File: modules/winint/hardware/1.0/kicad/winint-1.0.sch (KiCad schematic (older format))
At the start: 56 parts, among them J1 Screw_Terminal_01x09, J2 Screw_Terminal_01x09, J3 M12-5PIN, J4 RELAYS, K1 SANYOU_SRD_Form_C, K2 SANYOU_SRD_Form_C, Q1 2N2219, Q2 2N2219, SW1 INSTANCE, U1 PC817, U2 PC817, U3 PC817, U4 PC817, U5 PC817, U6 PC817, U7 Teensy_3.2, U8 TEC2-2411WI, U9 MCP2551-I-P

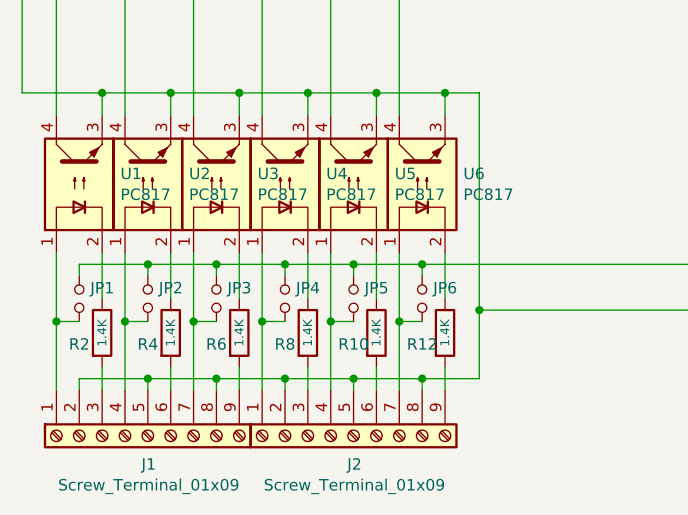
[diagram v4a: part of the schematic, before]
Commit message: Revised PCB layout
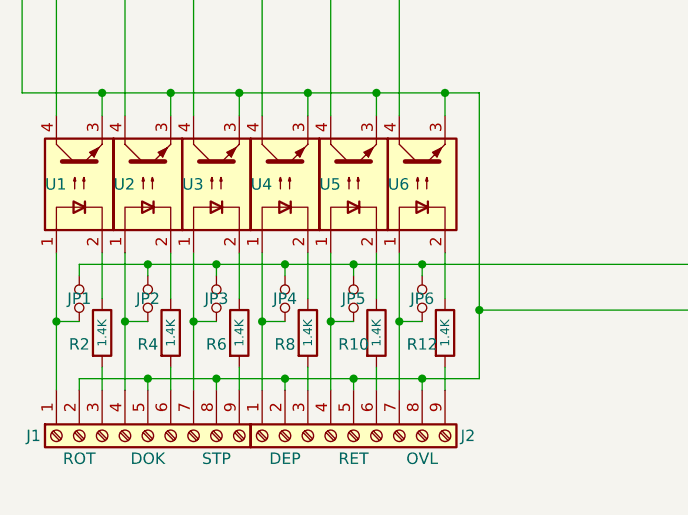
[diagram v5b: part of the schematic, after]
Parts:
- U1: value PC817 -> ROT
- U2: value PC817 -> DOK
- U3: value PC817 -> STP
- U4: value PC817 -> DEP
- U5: value PC817 -> RET
- U6: value PC817 -> OVL
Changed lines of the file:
@@
 U 1 1 60265696
 P 1100 6150
-F 0 "JP1" V 1146 6102 50  0000 R CNN
+F 0 "JP1" V 1100 6150 50  0000 C CNN
 F 1 "SCR" V 1055 6102 50  0001 R CNN
 F 2 "Connector_PinHeader_2.54mm:PinHeader_1x02_P2.54mm_Vertical" H 1100 6150 50  0001 C CNN
@@
 U 1 1 6026A113
 P 1400 6150
-F 0 "JP2" V 1446 6102 50  0000 R CNN
+F 0 "JP2" V 1400 6150 50  0000 C CNN
 F 1 "SCR" V 1355 6102 50  0001 R CNN
 F 2 "Connector_PinHeader_2.54mm:PinHeader_1x02_P2.54mm_Vertical" H 1400 6150 50  0001 C CNN
@@
 U 1 1 6026A739
 P 1700 6150
-F 0 "JP3" V 1746 6102 50  0000 R CNN
+F 0 "JP3" V 1700 6150 50  0000 C CNN
 F 1 "SCR" V 1655 6102 50  0001 R CNN
 F 2 "Connector_PinHeader_2.54mm:PinHeader_1x02_P2.54mm_Vertical" H 1700 6150 50  0001 C CNN
@@
 U 1 1 6026ABE4
 P 2000 6150
-F 0 "JP4" V 2046 6102 50  0000 R CNN
+F 0 "JP4" V 2000 6150 50  0000 C CNN
 F 1 "SCR" V 1955 6102 50  0001 R CNN
 F 2 "Connector_PinHeader_2.54mm:PinHeader_1x02_P2.54mm_Vertical" H 2000 6150 50  0001 C CNN
@@
 U 1 1 6026E0BA
 P 2300 6150
-F 0 "JP5" V 2346 6102 50  0000 R CNN
+F 0 "JP5" V 2300 6150 50  0000 C CNN
 F 1 "SCR" V 2255 6102 50  0001 R CNN
 F 2 "Connector_PinHeader_2.54mm:PinHeader_1x02_P2.54mm_Vertical" H 2300 6150 50  0001 C CNN
@@
 U 1 1 6026E6CF
 P 2600 6150
-F 0 "JP6" V 2646 6102 50  0000 R CNN
+F 0 "JP6" V 2600 6150 50  0000 C CNN
 F 1 "SCR" V 2555 6102 50  0001 R CNN
 F 2 "Connector_PinHeader_2.54mm:PinHeader_1x02_P2.54mm_Vertical" H 2600 6150 50  0001 C CNN
@@
 U 1 1 5FBA893A
 P 1400 6750
-F 0 "J1" V 1525 6746 50  0000 C CNN
-F 1 "Screw_Terminal_01x09" V 1616 6746 50  0000 C CNN
+F 0 "J1" V 1400 7250 50  0000 C CNN
+F 1 "Screw_Terminal_01x09" V 1616 6746 50  0001 C CNN
 F 2 "TerminalBlock_Phoenix:TerminalBlock_Phoenix_MPT-0,5-9-2.54_1x09_P2.54mm_Horizontal" H 1400 6750 50  0001 C CNN
 F 3 "~" H 1400 6750 50  0001 C CNN
@@
 U 1 1 5FBB1A89
 P 2300 6750
-F 0 "J2" V 2425 6746 50  0000 C CNN
-F 1 "Screw_Terminal_01x09" V 2516 6746 50  0000 C CNN
+F 0 "J2" V 2300 6250 50  0000 C CNN
+F 1 "Screw_Terminal_01x09" V 2516 6746 50  0001 C CNN
 F 2 "TerminalBlock_Phoenix:TerminalBlock_Phoenix_MPT-0,5-9-2.54_1x09_P2.54mm_Horizontal" H 2300 6750 50  0001 C CNN
 F 3 "~" H 2300 6750 50  0001 C CNN
@@
 U 1 1 5FBBA210
 P 1100 5650
-F 0 "U1" V 1146 5470 50  0000 R CNN
-F 1 "PC817" V 1055 5470 50  0000 R CNN
+F 0 "U1" V 1100 5800 50  0000 R CNN
+F 1 "ROT" V -100 5650 50  0000 C CNN
 F 2 "Package_DIP:DIP-4_W7.62mm" H 900 5450 50  0001 L CIN
 F 3 "http://www.soselectronic.cz/a_info/resource/d/pc817.pdf" H 1100 5650 50  0001 L CNN
@@
 U 1 1 5FBBFA82
 P 1400 5650
-F 0 "U2" V 1446 5470 50  0000 R CNN
-F 1 "PC817" V 1355 5470 50  0000 R CNN
+F 0 "U2" V 1400 5800 50  0000 R CNN
+F 1 "DOK" V 200 5650 50  0000 C CNN
 F 2 "Package_DIP:DIP-4_W7.62mm" H 1200 5450 50  0001 L CIN
 F 3 "http://www.soselectronic.cz/a_info/resource/d/pc817.pdf" H 1400 5650 50  0001 L CNN
@@
 U 1 1 5FBC043C
 P 1700 5650
-F 0 "U3" V 1746 5470 50  0000 R CNN
-F 1 "PC817" V 1655 5470 50  0000 R CNN
+F 0 "U3" V 1700 5800 50  0000 R CNN
+F 1 "STP" V 500 5650 50  0000 C CNN
 F 2 "Package_DIP:DIP-4_W7.62mm" H 1500 5450 50  0001 L CIN
 F 3 "http://www.soselectronic.cz/a_info/resource/d/pc817.pdf" H 1700 5650 50  0001 L CNN
@@
 U 1 1 5FBC0B0F
 P 2000 5650
-F 0 "U4" V 2046 5470 50  0000 R CNN
-F 1 "PC817" V 1955 5470 50  0000 R CNN
+F 0 "U4" V 2000 5800 50  0000 R CNN
+F 1 "DEP" V 800 5650 50  0000 C CNN
 F 2 "Package_DIP:DIP-4_W7.62mm" H 1800 5450 50  0001 L CIN
 F 3 "http://www.soselectronic.cz/a_info/resource/d/pc817.pdf" H 2000 5650 50  0001 L CNN
@@
 U 1 1 5FBC14DB
 P 2300 5650
-F 0 "U5" V 2346 5470 50  0000 R CNN
-F 1 "PC817" V 2255 5470 50  0000 R CNN
+F 0 "U5" V 2300 5800 50  0000 R CNN
+F 1 "RET" V 1100 5650 50  0000 C CNN
 F 2 "Package_DIP:DIP-4_W7.62mm" H 2100 5450 50  0001 L CIN
 F 3 "http://www.soselectronic.cz/a_info/resource/d/pc817.pdf" H 2300 5650 50  0001 L CNN
@@
 U 1 1 5FBC1BCF
 P 2600 5650
-F 0 "U6" V 2646 5470 50  0000 R CNN
-F 1 "PC817" V 2555 5470 50  0000 R CNN
+F 0 "U6" V 2600 5800 50  0000 R CNN
+F 1 "OVL" V 1400 5650 50  0000 C CNN
 F 2 "Package_DIP:DIP-4_W7.62mm" H 2400 5450 50  0001 L CIN
 F 3 "http://www.soselectronic.cz/a_info/resource/d/pc817.pdf" H 2600 5650 50  0001 L CNN
@@
 	4900 3300 5100 3300
 $Comp
-L power:GND #PWR?
+L power:GND #PWR0101
 U 1 1 5FD8D24E
 P 5000 6200
-F 0 "#PWR?" H 5000 5950 50  0001 C CNN
+F 0 "#PWR0101" H 5000 5950 50  0001 C CNN
 F 1 "GND" H 5005 6027 50  0000 C CNN
 F 2 "" H 5000 6200 50  0001 C CNN

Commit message: Tidy up
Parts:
- R15: value 200R, 125mW -> 200R
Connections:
- no-connect marks 2 -> 9
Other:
- moved on the sheet: SW1
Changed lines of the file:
@@
 U 1 1 5F1E6C5E
 P 7300 5600
-F 0 "R16" H 7400 5550 50  0000 C CNN
-F 1 "4K7" H 7450 5650 50  0000 C CNN
+F 0 "R16" H 7200 5450 50  0000 C CNN
+F 1 "4K7" V 7300 5600 39  0000 C CNN
 F 2 "Resistor_THT:R_Axial_DIN0204_L3.6mm_D1.6mm_P2.54mm_Vertical" V 7230 5600 50  0001 C CNN
 F 3 "~" H 7300 5600 50  0001 C CNN
@@
 U 1 1 5F21EFF3
 P 9100 5600
-F 0 "R20" H 9000 5550 50  0000 C CNN
-F 1 "100R" H 8950 5650 50  0000 C CNN
+F 0 "R20" H 9000 5450 50  0000 C CNN
+F 1 "100R" V 9100 5600 39  0000 C CNN
 F 2 "Resistor_THT:R_Axial_DIN0204_L3.6mm_D1.6mm_P5.08mm_Horizontal" V 9030 5600 50  0001 C CNN
 F 3 "~" H 9100 5600 50  0001 C CNN
@@
 U 1 1 5F21F397
 P 8700 5600
-F 0 "R19" H 8800 5650 50  0000 C CNN
-F 1 "100R" H 8850 5550 50  0000 C CNN
+F 0 "R19" H 8800 5750 50  0000 C CNN
+F 1 "100R" V 8700 5600 39  0000 C CNN
 F 2 "Resistor_THT:R_Axial_DIN0204_L3.6mm_D1.6mm_P5.08mm_Horizontal" V 8630 5600 50  0001 C CNN
 F 3 "~" H 8700 5600 50  0001 C CNN
@@
 	9100 4950 9100 5450
 Wire Wire Line
-	7300 6200 7400 6200
+	7300 6200 7100 6200
 Wire Wire Line
 	9100 6200 9100 6050
@@
 Connection ~ 7300 6200
 Wire Wire Line
-	950  1450 850  1450
-Wire Wire Line
-	850  1450 850  1550
-Wire Wire Line
-	950  1550 850  1550
-Connection ~ 850  1550
-Wire Wire Line
-	850  1550 850  1650
-Wire Wire Line
-	950  1650 850  1650
-Connection ~ 850  1650
-Wire Wire Line
-	850  1650 850  1750
-Wire Wire Line
-	950  1750 850  1750
-Connection ~ 850  1750
-Wire Wire Line
-	850  1750 850  1850
-Wire Wire Line
-	950  1850 850  1850
-Connection ~ 850  1850
-Wire Wire Line
-	850  1850 850  1950
-Wire Wire Line
-	950  1950 850  1950
-Connection ~ 850  1950
-Wire Wire Line
-	850  1950 850  2050
-Wire Wire Line
-	950  2050 850  2050
-Connection ~ 850  2050
-Wire Wire Line
 	9100 4350 9100 3650
 Wire Wire Line
 	9100 3650 8500 3650
 Wire Wire Line
-	7500 4050 7400 4050
+	7500 4050 7100 4050
 Connection ~ 8700 4750
 Connection ~ 9100 4950
@@
 Wire Wire Line
 	8500 4950 9100 4950
-Connection ~ 7400 6200
+Connection ~ 7100 6200
 Wire Wire Line
 	7500 3650 7200 3650
@@
 	7200 3650 7200 2900
 Connection ~ 7200 3650
-Wire Wire Line
-	7400 6200 8550 6200
 $Comp
 L Device:Polyfuse_Small F1
@@
 Connection ~ 6850 6200
 Wire Wire Line
-	6850 6200 7300 6200
+	6850 6200 7100 6200
 $Comp
 L Diode:1N4007 D4
 U 1 1 5F2ADAA6
 P 8200 2100
-F 0 "D4" H 8300 2150 50  0000 C CNN
-F 1 "1N4007" H 8200 2000 50  0000 C CNN
+F 0 "D4" H 8100 2050 50  0000 C CNN
+F 1 "1N4007" H 8000 2150 50  0000 C CNN
 F 2 "Diode_THT:D_DO-41_SOD81_P7.62mm_Horizontal" H 8200 1925 50  0001 C CNN
 F 3 "http://www.vishay.com/docs/88503/1n4001.pdf" H 8200 2100 50  0001 C CNN
@@
 U 1 1 5F2AF462
 P 9300 2100
-F 0 "D5" H 9400 2150 50  0000 C CNN
-F 1 "1N4007" H 9300 2000 50  0000 C CNN
+F 0 "D5" H 9200 2050 50  0000 C CNN
+F 1 "1N4007" H 9100 2150 50  0000 C CNN
 F 2 "Diode_THT:D_DO-41_SOD81_P7.62mm_Horizontal" H 9300 1925 50  0001 C CNN
 F 3 "http://www.vishay.com/docs/88503/1n4001.pdf" H 9300 2100 50  0001 C CNN
@@
 U 1 1 5F251E49
 P 7600 1400
-F 0 "D3" V 7500 1500 50  0000 R CNN
-F 1 "UP" V 7700 1400 50  0000 R CNN
+F 0 "D3" V 7700 1400 50  0000 R CNN
+F 1 "UP" V 7600 1550 50  0000 R CNN
 F 2 "LED_THT:LED_D3.0mm" H 7600 1400 50  0001 C CNN
 F 3 "~" H 7600 1400 50  0001 C CNN
@@
 U 1 1 5F252943
 P 7400 1400
-F 0 "D2" V 7300 1500 50  0000 R CNN
-F 1 "DN" V 7500 1400 50  0000 R CNN
+F 0 "D2" V 7500 1400 50  0000 R CNN
+F 1 "DN" V 7400 1550 50  0000 R CNN
 F 2 "LED_THT:LED_D3.0mm" H 7400 1400 50  0001 C CNN
 F 3 "~" H 7400 1400 50  0001 C CNN
@@
 U 1 1 5F28093B
 P 7600 1100
-F 0 "R18" V 7500 1100 50  0000 C CNN
+F 0 "R18" H 7500 950 50  0000 C CNN
 F 1 "200R" V 7600 1100 50  0000 C CNN
 F 2 "Resistor_THT:R_Axial_DIN0204_L3.6mm_D1.6mm_P5.08mm_Horizontal" V 7530 1100 50  0001 C CNN
@@
 U 1 1 5F285FEA
 P 7400 1100
-F 0 "R17" V 7300 1100 50  0000 C CNN
+F 0 "R17" H 7300 950 50  0000 C CNN
 F 1 "200R" V 7400 1100 50  0000 C CNN
 F 2 "Resistor_THT:R_Axial_DIN0204_L3.6mm_D1.6mm_P5.08mm_Horizontal" V 7330 1100 50  0001 C CNN
@@
 U 1 1 5F2B75CF
 P 6200 2900
-F 0 "R15" V 6100 2900 50  0000 C CNN
-F 1 "200R, 125mW" V 6280 2900 39  0000 C CNN
+F 0 "R15" V 6300 2900 50  0000 C CNN
+F 1 "200R" V 6200 2900 39  0000 C CNN
 F 2 "Resistor_THT:R_Axial_DIN0204_L3.6mm_D1.6mm_P5.08mm_Horizontal" V 6130 2900 50  0001 C CNN
 F 3 "~" H 6200 2900 50  0001 C CNN
@@
 U 1 1 5F337256
 P 9300 1500
-F 0 "K2" V 9867 1500 50  0000 C CNN
-F 1 "SANYOU_SRD_Form_C" V 9776 1500 50  0000 C CNN
+F 0 "K2" V 9750 1500 50  0000 C CNN
+F 1 "SANYOU_SRD_Form_C" V 9776 1500 50  0001 C CNN
 F 2 "PDJR:RS_RELAY_476-757" H 9750 1450 50  0001 L CNN
 F 3 "" H 9300 1500 50  0001 C CNN
@@
 U 1 1 5F33E00B
 P 8200 1500
-F 0 "K1" V 8767 1500 50  0000 C CNN
-F 1 "SANYOU_SRD_Form_C" V 8676 1500 50  0000 C CNN
+F 0 "K1" V 8650 1500 50  0000 C CNN
+F 1 "SANYOU_SRD_Form_C" V 8676 1500 50  0001 C CNN
 F 2 "PDJR:RS_RELAY_476-757" H 8650 1450 50  0001 L CNN
 F 3 "" H 8200 1500 50  0001 C CNN
@@
 U 1 1 5F3B6D27
 P 5850 2900
-F 0 "D1" H 6010 2850 50  0000 R CNN
-F 1 "PWR/TX" H 6200 2950 50  0000 R CNN
+F 0 "D1" H 5900 2800 50  0000 R CNN
+F 1 "PWR/TX" H 6000 3000 50  0000 R CNN
 F 2 "LED_THT:LED_D3.0mm" H 5850 2900 50  0001 C CNN
 F 3 "~" H 5850 2900 50  0001 C CNN
@@
 U 1 1 5F38A0E7
 P 4350 4300
-F 0 "C1" V 4300 4200 50  0000 R CNN
-F 1 "100nF" V 4300 4600 50  0000 R CNN
+F 0 "C1" V 4400 4250 50  0000 R CNN
+F 1 "100nF" V 4300 4250 50  0000 R CNN
 F 2 "Capacitor_THT:CP_Radial_D5.0mm_P2.50mm" H 4388 4150 50  0001 C CNN
 F 3 "~" H 4350 4300 50  0001 C CNN
@@
 U 1 1 5F37EE82
 P 9500 5600
-F 0 "JP7" V 9546 5552 50  0000 R CNN
-F 1 "SCR" V 9455 5552 50  0000 R CNN
+F 0 "JP7" V 9650 5550 50  0000 R CNN
+F 1 "SCR" V 9400 5550 50  0000 R CNN
 F 2 "Connector_PinHeader_2.54mm:PinHeader_1x02_P2.54mm_Vertical" H 9500 5600 50  0001 C CNN
 F 3 "~" H 9500 5600 50  0001 C CNN
@@
 L Switch:SW_DIP_x07 SW1
 U 1 1 5F60BF0B
-P 1250 1850
-F 0 "SW1" H 1250 2517 50  0000 C CNN
-F 1 "INSTANCE" H 1250 2426 50  0000 C CNN
-F 2 "Package_DIP:DIP-14_W7.62mm" H 1250 1850 50  0001 C CNN
-F 3 "~" H 1250 1850 50  0001 C CNN
-	1    1250 1850
+P 1250 3100
+F 0 "SW1" H 1250 3767 50  0000 C CNN
+F 1 "INSTANCE" H 1250 3676 50  0000 C CNN
+F 2 "Package_DIP:DIP-14_W7.62mm" H 1250 3100 50  0001 C CNN
+F 3 "~" H 1250 3100 50  0001 C CNN
+	1    1250 3100
 	1    0    0    -1
 $EndComp
@@
 	8550 6200 8700 6200
 Wire Wire Line
-	7400 4050 7400 6200
+	7100 4050 7100 6200
 Wire Wire Line
 	1100 6550 1100 6500
@@
 	1200 5250 850  5250
 Connection ~ 1200 5250
-Wire Wire Line
-	850  2050 850  5250
 $Comp
 L Device:R R3
@@
 	5000 6200 6850 6200
 Wire Wire Line
-	1550 1450 3600 1450
-Wire Wire Line
-	3600 1450 3600 2700
-Wire Wire Line
-	3600 2700 3800 2700
-Wire Wire Line
-	3800 2800 3500 2800
-Wire Wire Line
-	3500 2800 3500 1550
-Wire Wire Line
-	3500 1550 1550 1550
-Wire Wire Line
-	1550 1650 3400 1650
-Wire Wire Line
-	3400 1650 3400 2900
-Wire Wire Line
-	3400 2900 3800 2900
-Wire Wire Line
-	3800 3000 3300 3000
-Wire Wire Line
-	3300 3000 3300 1750
-Wire Wire Line
-	3300 1750 1550 1750
-Wire Wire Line
-	1550 1850 3200 1850
-Wire Wire Line
-	3200 1850 3200 3100
-Wire Wire Line
-	3200 3100 3800 3100
-Wire Wire Line
-	3800 3200 3100 3200
-Wire Wire Line
-	3100 3200 3100 1950
-Wire Wire Line
-	3100 1950 1550 1950
-Wire Wire Line
-	1550 2050 3000 2050
-Wire Wire Line
-	3000 2050 3000 3300
-Wire Wire Line
-	3000 3300 3800 3300
-Wire Wire Line
 	1000 4300 3100 4300
 Wire Wire Line
@@
 Wire Wire Line
 	3700 4300 4200 4300
-Wire Wire Line
-	3700 4000 3700 750
 Wire Wire Line
 	3700 750  7200 750
@@
 	1    0    0    -1
 $EndComp
+NoConn ~ 4900 2700
+NoConn ~ 4900 2800
+NoConn ~ 4900 2900
+NoConn ~ 4900 3000
+NoConn ~ 4900 3100
+NoConn ~ 4900 3200
+NoConn ~ 3800 3800
+Wire Wire Line
+	7300 6200 8550 6200
+Wire Wire Line
+	3700 750  3700 4000
+Wire Wire Line
+	3800 2700 1550 2700
+Wire Wire Line
+	1550 2800 3800 2800
+Wire Wire Line
+	3800 2900 1550 2900
+Wire Wire Line
+	1550 3000 3800 3000
+Wire Wire Line
+	3800 3100 1550 3100
+Wire Wire Line
+	1550 3200 3800 3200
+Wire Wire Line
+	3800 3300 1550 3300
+Wire Wire Line
+	850  2700 950  2700
+Wire Wire Line
+	850  2700 850  2800
+Wire Wire Line
+	950  2800 850  2800
+Connection ~ 850  2800
+Wire Wire Line
+	850  2800 850  2900
+Wire Wire Line
+	950  2900 850  2900
+Connection ~ 850  2900
+Wire Wire Line
+	850  2900 850  3000
+Wire Wire Line
+	950  3000 850  3000
+Connection ~ 850  3000
+Wire Wire Line
+	850  3000 850  3100
+Wire Wire Line
+	950  3100 850  3100
+Connection ~ 850  3100
+Wire Wire Line
+	850  3100 850  3200
+Wire Wire Line
+	950  3200 850  3200
+Connection ~ 850  3200
+Wire Wire Line
+	850  3200 850  3300
+Wire Wire Line
+	950  3300 850  3300
+Connection ~ 850  3300
+Wire Wire Line
+	850  3300 850  5250
 $EndSCHEMATC
